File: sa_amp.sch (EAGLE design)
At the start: 87 parts, among them U4 TPA3255

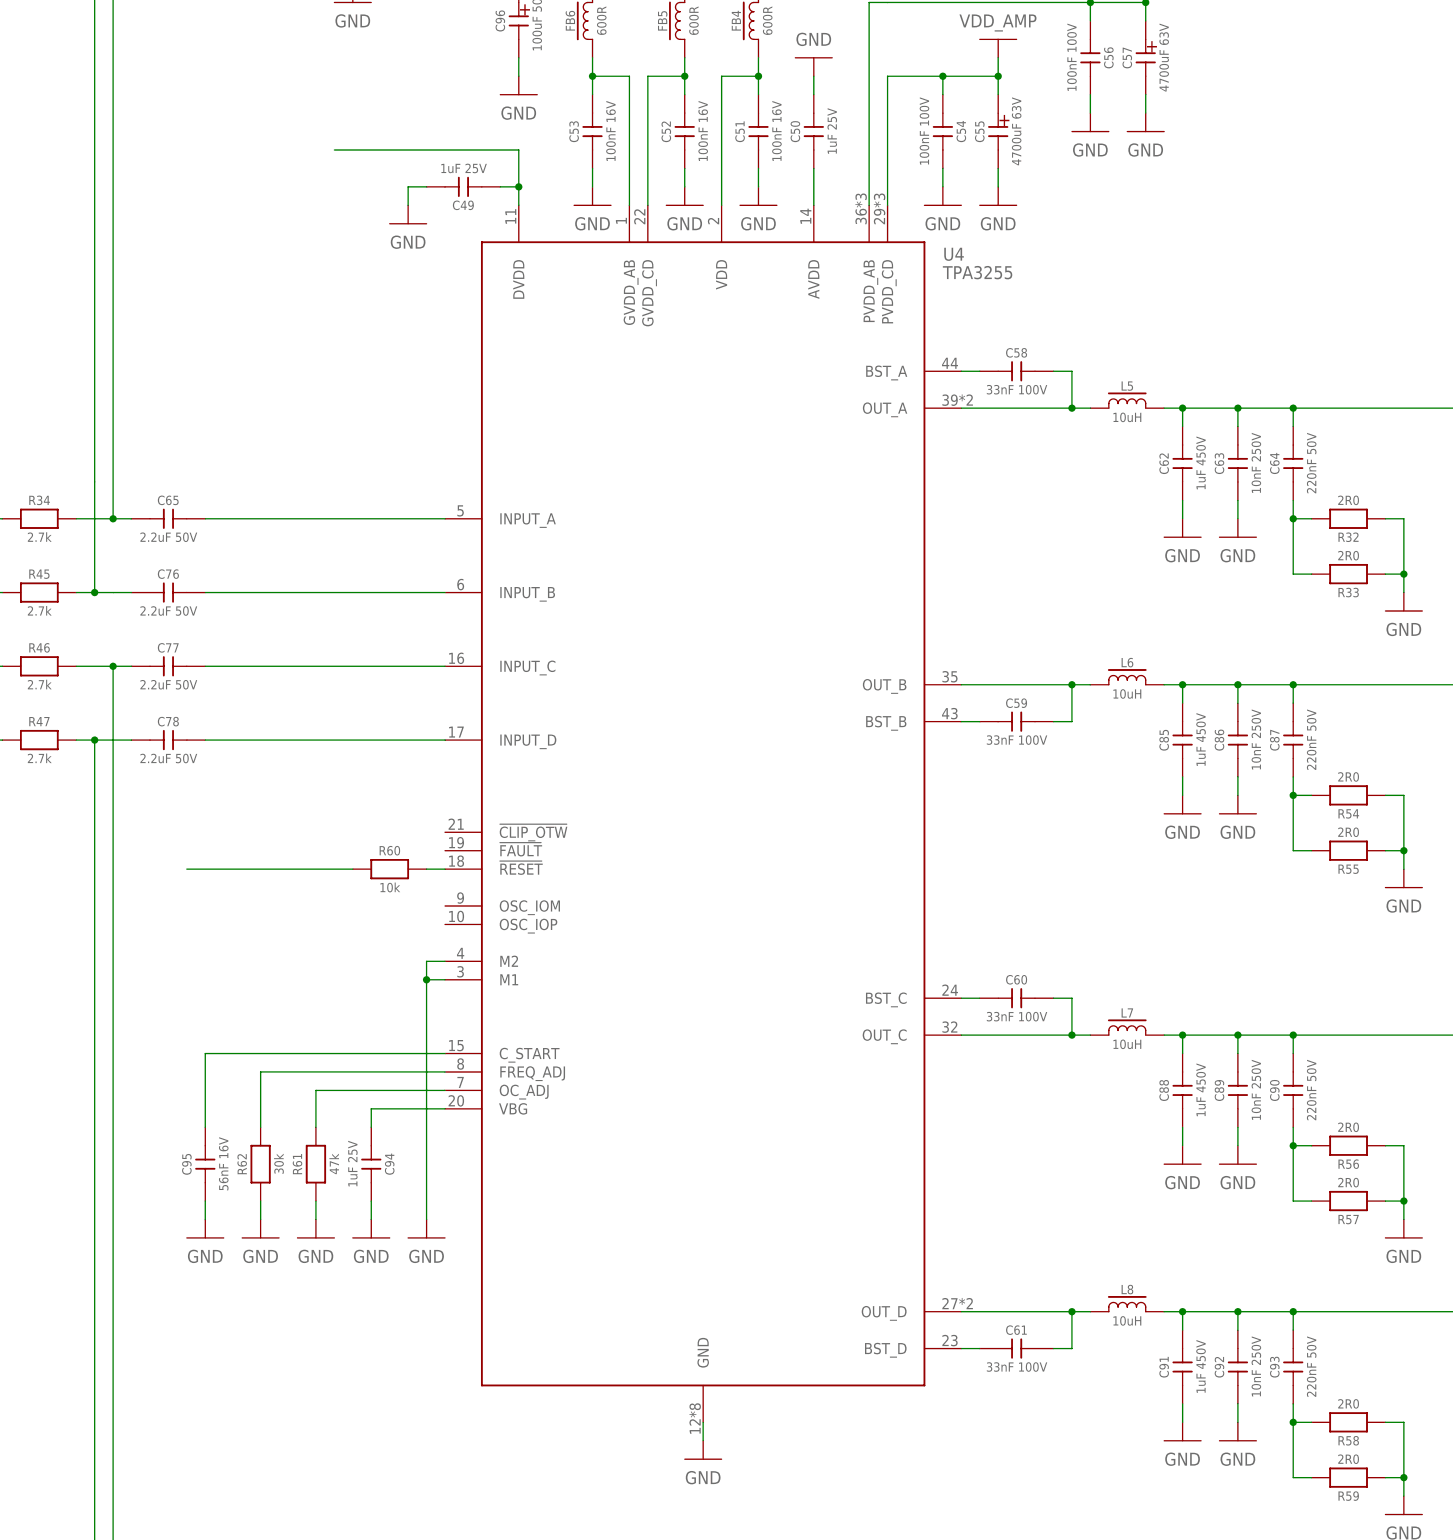
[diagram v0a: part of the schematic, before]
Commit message: Amplifier modules ready to be made
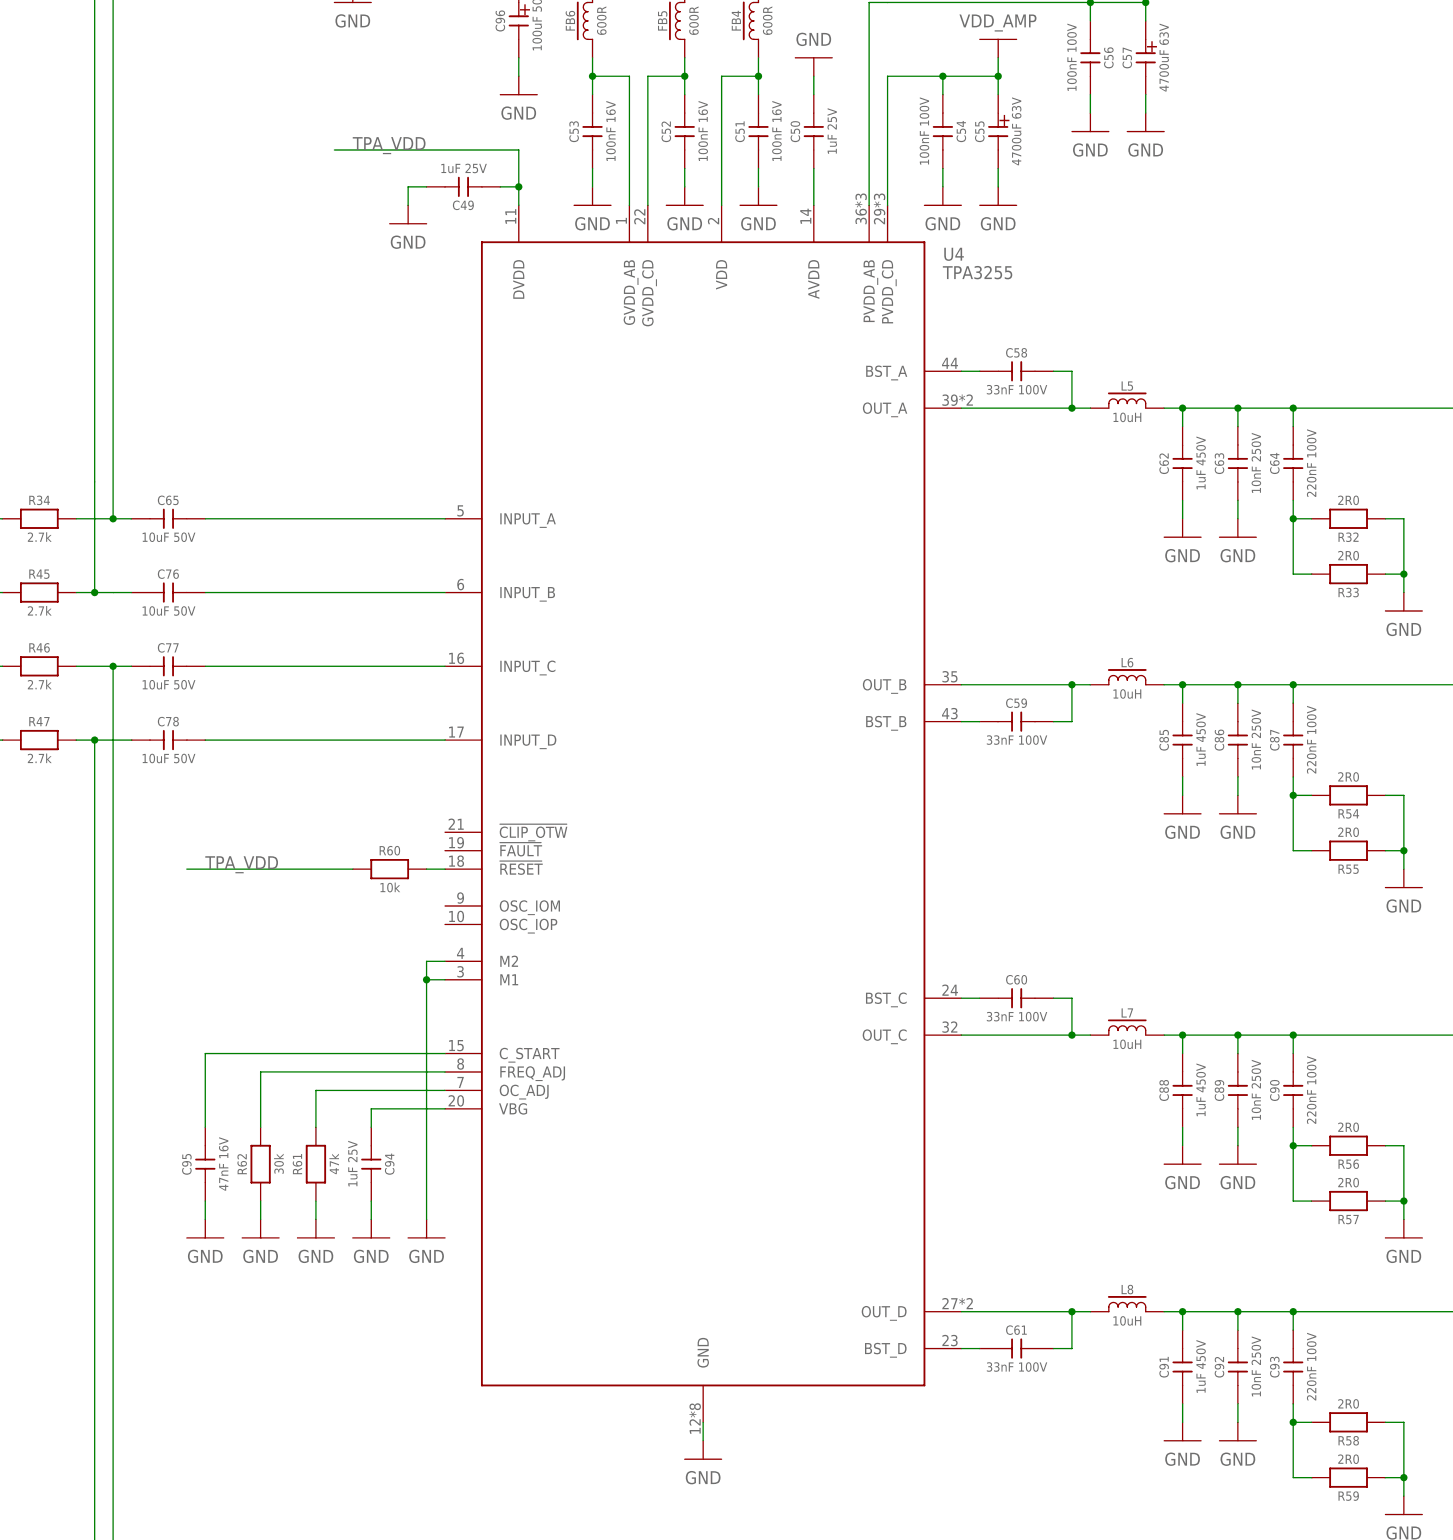
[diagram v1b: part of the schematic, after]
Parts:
- C64, C87, C90, C93: value 220nF 50V -> 220nF 100V; device CAPACITORS:C1608X7R1H224K080AB -> CAPACITORS:C3216X7R2A224K115AA
- C65, C76, C77, C78: value 2.2uF 50V -> 10uF 50V; device CAPACITORS:MKS2B042201F00KSSD -> CAPACITORS:MKS2B051001N00JSSD
- C95: value 56nF 16V -> 47nF 16V; device CAPACITORS:GRM188R71C563JA01D -> CAPACITORS:CL10B473KO8NNNC
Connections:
- net TPA_VDD_1 renamed TPA_VDD
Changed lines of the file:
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@@
 <part name="R32" library="RESISTORS" deviceset="CRCW12062R00FNEA" device="" value="2R0"/>
 <part name="R33" library="RESISTORS" deviceset="CRCW12062R00FNEA" device="" value="2R0"/>
-<part name="C64" library="CAPACITORS" deviceset="C1608X7R1H224K080AB" device="" value="220nF 50V"/>
+<part name="C64" library="CAPACITORS" deviceset="C3216X7R2A224K115AA" device="" value="220nF 100V"/>
 <part name="R34" library="r_0603" deviceset="ERJ3EKF2701V" device="" value="2.7k"/>
-<part name="C65" library="CAPACITORS" deviceset="MKS2B042201F00KSSD" device="" value="2.2uF 50V"/>
+<part name="C65" library="CAPACITORS" deviceset="MKS2B051001N00JSSD" device="" value="10uF 50V"/>
 <part name="R35" library="r_0603" deviceset="ERJ3EKF3302V" device="" value="33k"/>
 <part name="R36" library="r_0603" deviceset="ERJ3EKF1002V" device="" value="10k"/>
@@
 <part name="GND54" library="NETS" deviceset="GND" device=""/>
 <part name="R45" library="r_0603" deviceset="ERJ3EKF2701V" device="" value="2.7k"/>
-<part name="C76" library="CAPACITORS" deviceset="MKS2B042201F00KSSD" device="" value="2.2uF 50V"/>
+<part name="C76" library="CAPACITORS" deviceset="MKS2B051001N00JSSD" device="" value="10uF 50V"/>
 <part name="R46" library="r_0603" deviceset="ERJ3EKF2701V" device="" value="2.7k"/>
-<part name="C77" library="CAPACITORS" deviceset="MKS2B042201F00KSSD" device="" value="2.2uF 50V"/>
+<part name="C77" library="CAPACITORS" deviceset="MKS2B051001N00JSSD" device="" value="10uF 50V"/>
 <part name="R47" library="r_0603" deviceset="ERJ3EKF2701V" device="" value="2.7k"/>
-<part name="C78" library="CAPACITORS" deviceset="MKS2B042201F00KSSD" device="" value="2.2uF 50V"/>
+<part name="C78" library="CAPACITORS" deviceset="MKS2B051001N00JSSD" device="" value="10uF 50V"/>
 <part name="R48" library="r_0603" deviceset="ERJ3EKF3302V" device="" value="33k"/>
 <part name="R49" library="r_0603" deviceset="ERJ3EKF1002V" device="" value="10k"/>
@@
 <part name="R54" library="RESISTORS" deviceset="CRCW12062R00FNEA" device="" value="2R0"/>
 <part name="R55" library="RESISTORS" deviceset="CRCW12062R00FNEA" device="" value="2R0"/>
-<part name="C87" library="CAPACITORS" deviceset="C1608X7R1H224K080AB" device="" value="220nF 50V"/>
+<part name="C87" library="CAPACITORS" deviceset="C3216X7R2A224K115AA" device="" value="220nF 100V"/>
 <part name="C88" library="CAPACITORS" deviceset="ECWFE2W105K" device="" value="1uF 450V"/>
 <part name="GND69" library="NETS" deviceset="GND" device=""/>
@@
 <part name="R56" library="RESISTORS" deviceset="CRCW12062R00FNEA" device="" value="2R0"/>
 <part name="R57" library="RESISTORS" deviceset="CRCW12062R00FNEA" device="" value="2R0"/>
-<part name="C90" library="CAPACITORS" deviceset="C1608X7R1H224K080AB" device="" value="220nF 50V"/>
+<part name="C90" library="CAPACITORS" deviceset="C3216X7R2A224K115AA" device="" value="220nF 100V"/>
 <part name="C91" library="CAPACITORS" deviceset="ECWFE2W105K" device="" value="1uF 450V"/>
 <part name="GND72" library="NETS" deviceset="GND" device=""/>
@@
 <part name="R58" library="RESISTORS" deviceset="CRCW12062R00FNEA" device="" value="2R0"/>
 <part name="R59" library="RESISTORS" deviceset="CRCW12062R00FNEA" device="" value="2R0"/>
-<part name="C93" library="CAPACITORS" deviceset="C1608X7R1H224K080AB" device="" value="220nF 50V"/>
+<part name="C93" library="CAPACITORS" deviceset="C3216X7R2A224K115AA" device="" value="220nF 100V"/>
 <part name="GND75" library="NETS" deviceset="GND" device=""/>
 <part name="R60" library="r_0603" deviceset="ERJ3EKF1002V" device="" value="10k"/>
@@
 <part name="R62" library="r_0603" deviceset="ERJ3EKF3002V" device="" value="30k"/>
 <part name="GND78" library="NETS" deviceset="GND" device=""/>
-<part name="C95" library="CAPACITORS" deviceset="GRM188R71C563JA01D" device="" value="56nF 16V"/>
+<part name="C95" library="CAPACITORS" deviceset="CL10B473KO8NNNC" device="" value="47nF 16V"/>
 <part name="GND79" library="NETS" deviceset="GND" device=""/>
 <part name="GND80" library="NETS" deviceset="GND" device=""/>
@@
 </segment>
 </net>
-<net name="TPA_VDD_1" class="0">
+<net name="TPA_VDD" class="0">
 <segment>
 <pinref part="U4" gate="G$1" pin="DVDD"/>
@@
 <junction x="261.62" y="271.78"/>
 <wire x1="261.62" y1="276.86" x2="236.22" y2="276.86" width="0.1524" layer="91"/>
+<label x="238.76" y="276.86" size="1.778" layer="95"/>
 </segment>
 <segment>
 <pinref part="R60" gate="G$1" pin="1"/>
 <wire x1="238.76" y1="177.8" x2="215.9" y2="177.8" width="0.1524" layer="91"/>
-</segment>
-</net>
+<label x="218.44" y="177.8" size="1.778" layer="95"/>
+</segment>
+</net>
